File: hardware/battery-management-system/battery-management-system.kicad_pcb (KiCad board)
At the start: 4 copper layers, 100 x 100 mm, 195 parts, among them IC1 LT8584EFE#PBF, IC2 LT8584EFE#PBF, IC3 LT8584EFE#PBF, IC4 LT8584EFE#PBF, J1 VBAT_DISCHARGE, J10 TEMP_CELL4, J2 CELLS, J3 Charge, J4 Discharge, J5 AMPHENOL_micro_usb_10118194-0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, J6 ARM-JTAG-SWD, J7 TEMP_CELL1, J8 TEMP_CELL2, J9 TEMP_CELL3, Q1 TJ40S04M3L, Q10 BS250FTA, Q11 BS250FTA, Q12 BS250FTA, Q13 BS250FTA, Q14 DMN3404L, Q2 TJ40S04M3L, Q3 DMN3404L, Q4 DMN3404L, Q5 DMN3404L, Q6 DMN3404L, Q7 DMN3404L, Q8 BS250FTA, Q9 DMN3404L, T1 NA6252-ALD, T2 NA6252-ALD, T3 NA6252-ALD, T4 NA6252-ALD, U1 STC3100, U10 LM2904M8-13, U11 LM2904M8-13, U2 L6982CDR, U3 L6982CDR, U4 ICL7660, U5 ICL7660, U6 FT230XS, U7 STM32L071CZTx, U8 AT24C512C, U9 NCT75DR2G

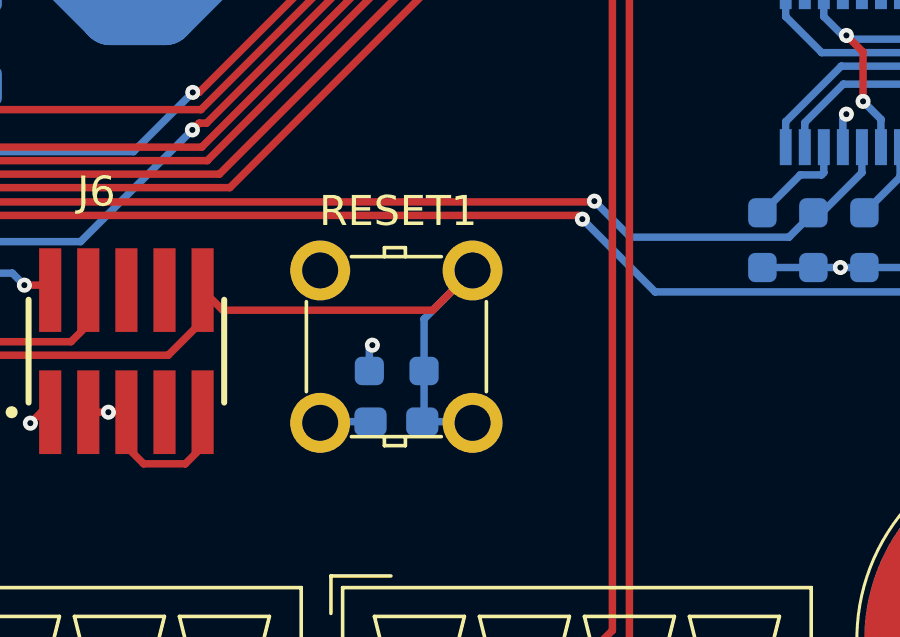
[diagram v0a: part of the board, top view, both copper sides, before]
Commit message: replace reset button, update symbols
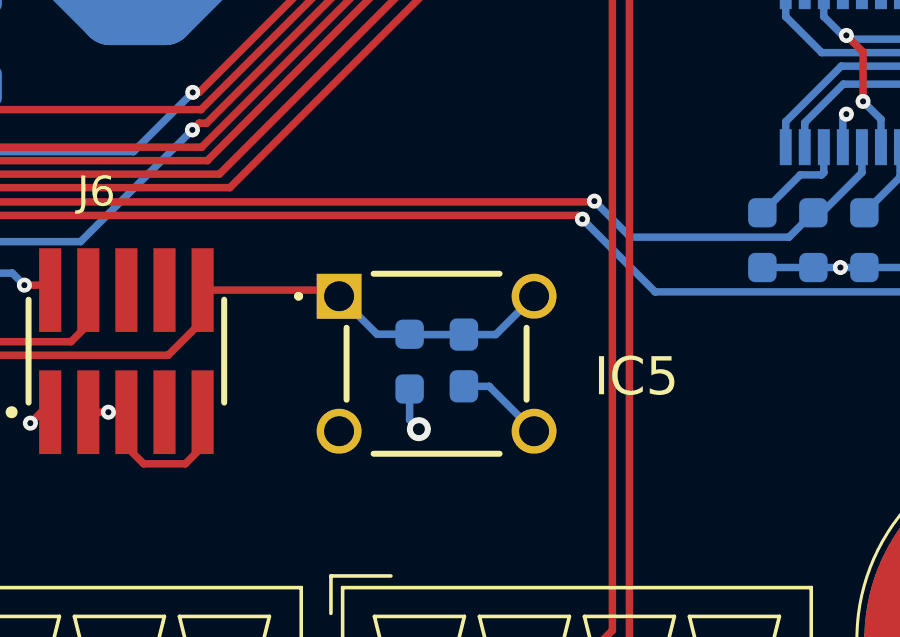
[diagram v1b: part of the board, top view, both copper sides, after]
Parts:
- removed RESET1: TMG1-01, benediktibk:TMG1-01
- added IC5: RESET, benediktibk:TS026650BK100SCRD, F.Cu at (88.1, 100.6)
- moved C29 3.04 mm to (92.2, 102.7), turned to -90 degrees
- moved R24 0.53 mm to (90.4, 102.8), turned to 90 degrees
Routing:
- net /MCU/NRST: track 42.4 -> 37.3 mm
- net GND: track 190.1 -> 191.4 mm
- net /3V3: track 54.5 -> 55.1 mm

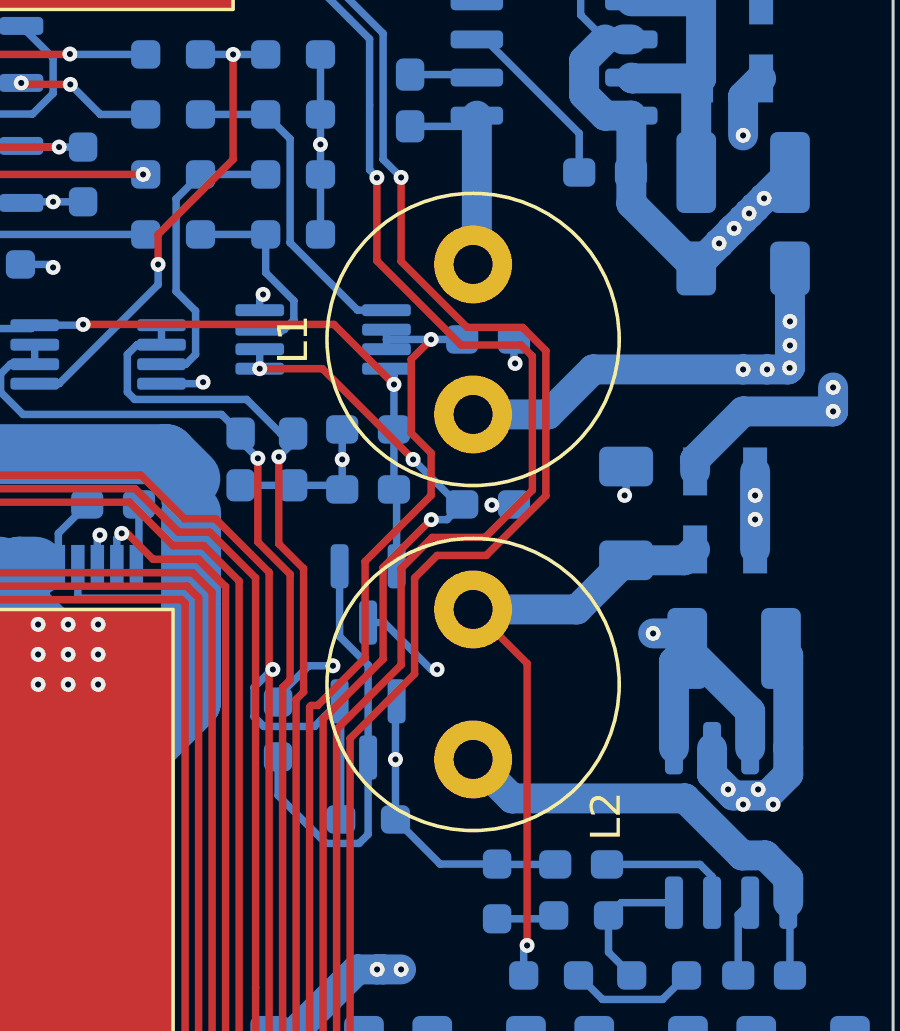
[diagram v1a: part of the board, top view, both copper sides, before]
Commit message: replace inductance of power supplies
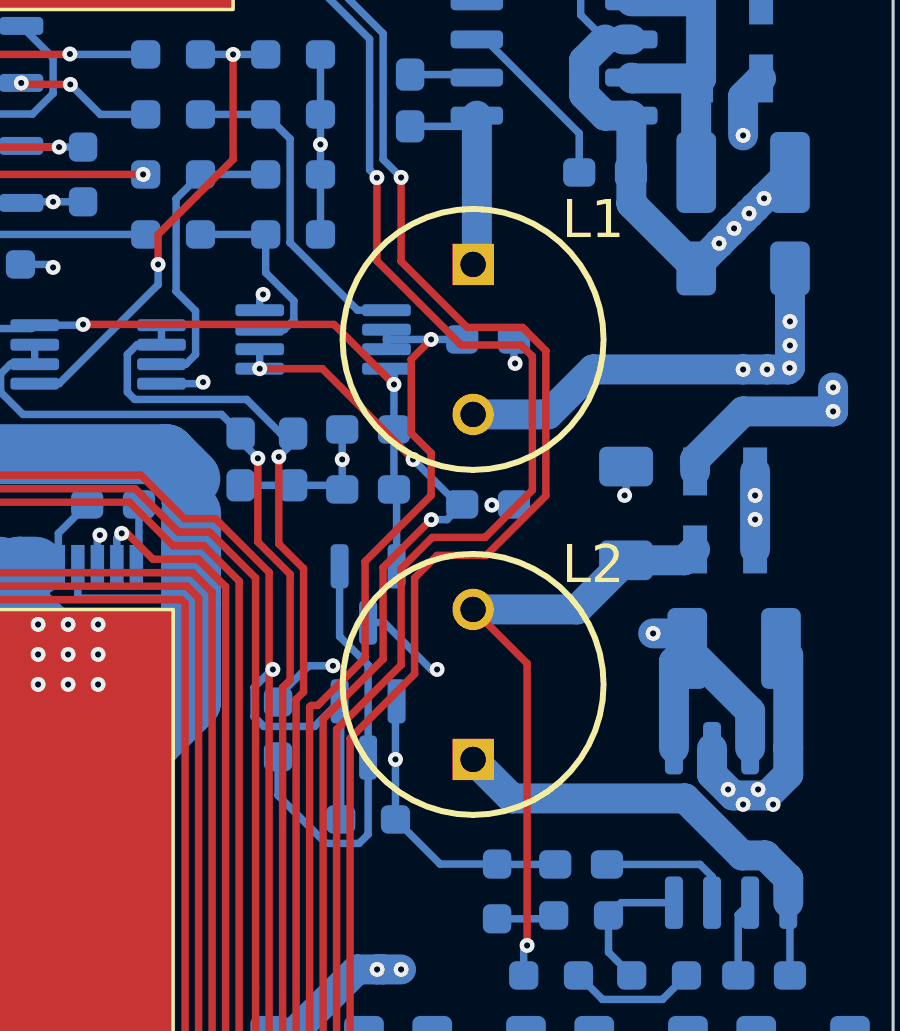
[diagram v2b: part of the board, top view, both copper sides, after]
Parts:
- L1, L2: value 22uH -> RLB0914-220KL; footprint benediktibk:L_Radial_D9.5mm_P5.00mm_Fastron_07HVP -> benediktibk:RLB0914220KL
- moved L1 5.00 mm to (106.0, 48.5), turned to -90 degrees
- moved L2 5.00 mm to (106.0, 65.0), turned to 90 degrees
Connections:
- L1 pad 1: /3V3 -> Net-(U2-SW)
- L1 pad 2: Net-(U2-SW) -> /3V3
- L2 pad 1: Net-(D6-A) -> Net-(U3-SW)
- L2 pad 2: Net-(U3-SW) -> Net-(D6-A)
